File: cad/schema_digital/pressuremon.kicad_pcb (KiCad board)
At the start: 2 copper layers, 50 x 50 mm, 16 parts, among them J1 Digital Pressure 1, J2 Digital Pressure 2, Q1 BC337, U3 DS18B20

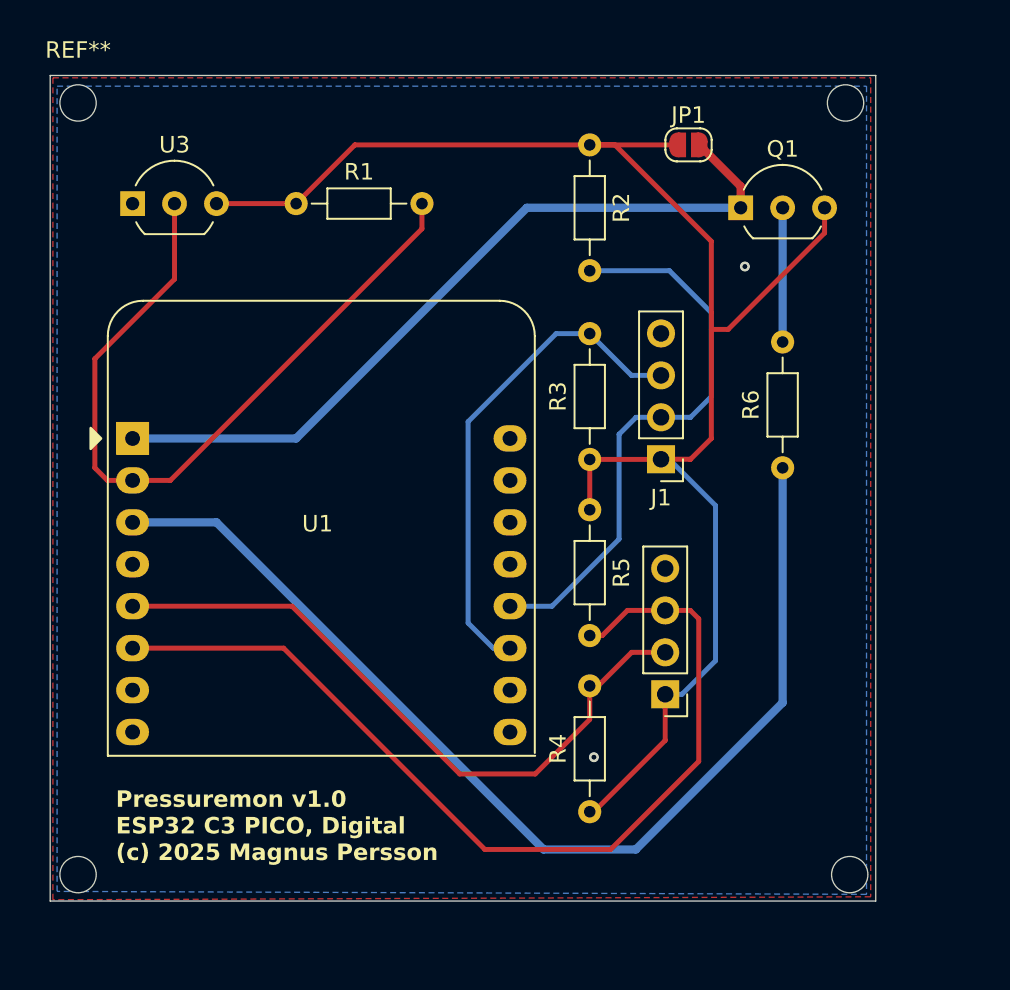
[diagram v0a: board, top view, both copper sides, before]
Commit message: Update pcb for digital sensors
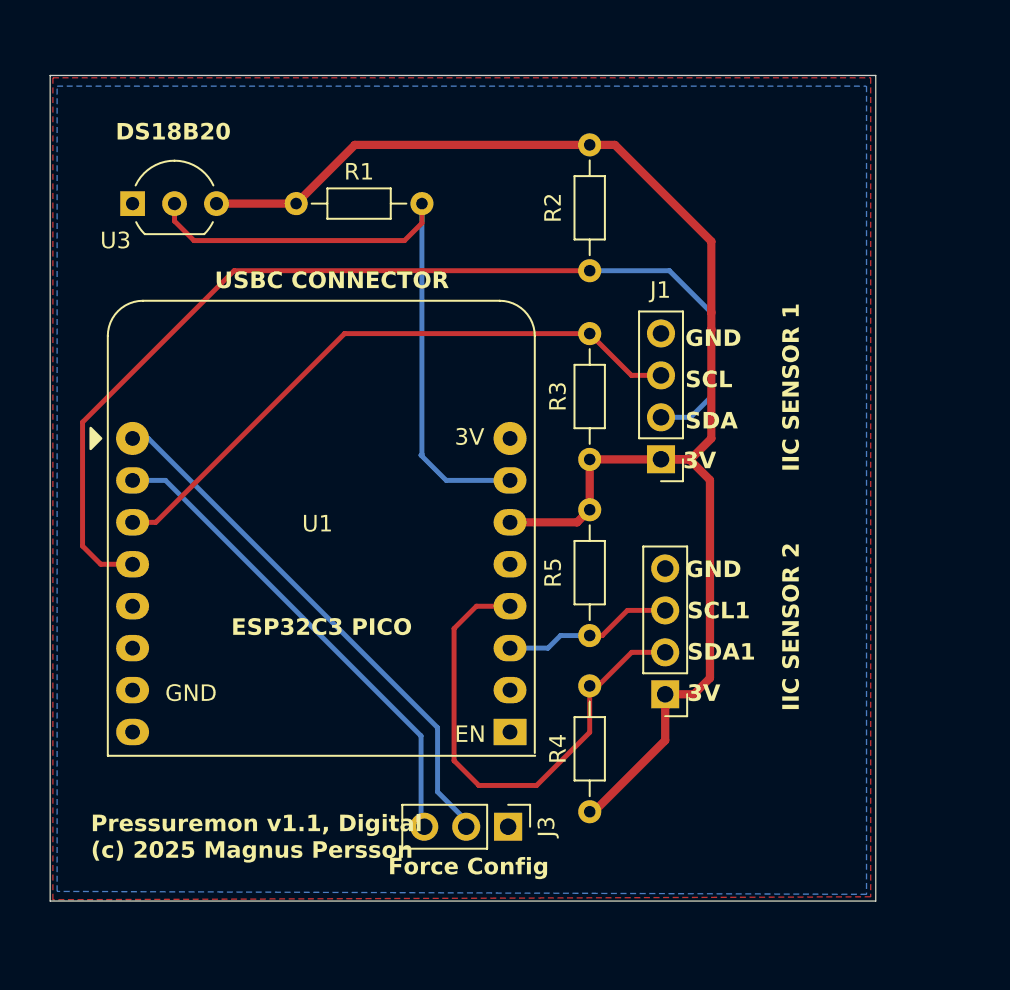
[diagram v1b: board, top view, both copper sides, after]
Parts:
- removed ? (x3): , 
- removed JP1: SolderJumper_2_Open, Jumper:SolderJumper-2_P1.3mm_Open_RoundedPad1.0x1.5mm
- removed Q1: BC337, Package_TO_SOT_THT:TO-92_Inline_Wide
- removed R6: 3.3k, Resistor_THT:R_Axial_DIN0204_L3.6mm_D1.6mm_P7.62mm_Horizontal
- removed REF**: MountingHole_2.2mm_M2, MountingHole:MountingHole_2.2mm_M2
- added J3: Force Config, Connector_PinHeader_2.54mm:PinHeader_1x03_P2.54mm_Vertical, F.Cu at (135.8, 86.0)
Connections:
- U1 pad 1: +3.3V -> unconnected-(U1-3.3V-Pad1)
- U1 pad 15: unconnected-(U1-RX-Pad15) -> Net-(J3-Pin_3)
- U1 pad 16: unconnected-(U1-TX-Pad16) -> Net-(J3-Pin_2)
- U1 pad 3: Net-(U1-4(MOSI)) -> /VCC
- U1 pad 9: +5V -> unconnected-(U1-5V-Pad9)
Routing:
- net Net-(U1-4(MOSI)): track 65.5 -> 0.00 mm
- net +3.3V: track 47.5 -> 0.00 mm
- net /SCL1: track 57.6 -> 10.3 mm
- net Net-(J3-Pin_2): track 0.00 -> 32.9 mm
- net Net-(J3-Pin_3): track 0.00 -> 30.0 mm
- net /SDA: track 34.7 -> 62.6 mm
- net /SDA1: track 40.7 -> 30.3 mm
- net /VCC: track 99.8 -> 89.7 mm
- net Net-(Q1-B): track 8.13 -> 0.00 mm
- net /SCL: track 30.3 -> 37.8 mm
- net Net-(U1-5): track 46.0 -> 39.4 mm
- net GND: vias 2 -> 0
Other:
- board text added: "3V"
- board text added: "DS18B20"
- board text added: "ESP32C3 PICO"
- board text added: "Force Config"
- board text added: "GND"
- board text added: "IIC SENSOR 1"
- board text added: "IIC SENSOR 2"
- board text added: "Pressuremon v1.1, Digital (c) 2025 Magnus Persson"
- board text added: "SCL"
- board text added: "SCL1"
- board text added: "SDA"
- board text added: "SDA1"
- board text added: "USBC CONNECTOR"
- board text removed: "Pressuremon v1.0 ESP32 C3 PICO, Digital (c) 2025 Magnus Persson"

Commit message: Update pcb
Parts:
- added ?: , , F.Cu at (156.0, 42.5)
- added ?: , , F.Cu at (110.0, 88.5)
- added ?: , , F.Cu at (156.0, 88.5)
- added REF**: MountingHole_2.2mm_M2_ISO7380, MountingHole:MountingHole_2.2mm_M2_ISO7380, F.Cu at (110.0, 42.5)
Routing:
- net /SDA1: track 30.3 -> 13.3 mm
- net Net-(U1-5): track 39.4 -> 38.5 mm
- net /SDA: track 62.6 -> 61.9 mm
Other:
- board text added: "I2C SENSOR 1"
- board text added: "I2C SENSOR 2"
- board text removed: "IIC SENSOR 1"
- board text removed: "IIC SENSOR 2"

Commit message: Update pcb to v1.2
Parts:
- removed ? (x3): , 
- removed REF**: MountingHole_2.2mm_M2_ISO7380, MountingHole:MountingHole_2.2mm_M2_ISO7380
- J1: value Digital Pressure 1 -> Conn_01x04_Pin
- J2: value Digital Pressure 2 -> Conn_01x04_Pin
- J3: value Force Config -> Conn_01x03_Pin
- R1, R2, R3, R4, R5: value 3.3k -> R
- U3: footprint Package_TO_SOT_THT:TO-92_Inline_Wide -> Package_TO_SOT_THT:TO-92_Inline
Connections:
- U1 pad 10: GND -> Net-(J3-Pin_3)
- U1 pad 11: unconnected-(U1-6-Pad11) -> /SCL
- U1 pad 12: unconnected-(U1-7(LED)-Pad12) -> /SDA
- U1 pad 13: /SDA -> unconnected-(U1-7(LED)-Pad13)
- U1 pad 14: /SCL -> unconnected-(U1-6-Pad14)
- U1 pad 15: Net-(J3-Pin_3) -> GND
- U1 pad 16: Net-(J3-Pin_2) -> unconnected-(U1-5V-Pad16)
- U1 pad 9: unconnected-(U1-5V-Pad9) -> Net-(J3-Pin_2)
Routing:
- net /SDA: track 61.9 -> 52.5 mm
- net Net-(J3-Pin_3): track 30.0 -> 21.4 mm
- net Net-(J3-Pin_2): track 32.9 -> 24.8 mm
- net /SCL: track 37.8 -> 40.9 mm
- net /VCC: track 89.7 -> 92.2 mm
- net Net-(U1-5): track 38.5 -> 40.1 mm
- net unconnected-(U1-5V-Pad16): track 0.00 -> 0.95 mm
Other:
- board text added: "Pressuremon v1.2, Digital (c) 2025 Magnus Persson"
- board text removed: "Pressuremon v1.1, Digital (c) 2025 Magnus Persson"

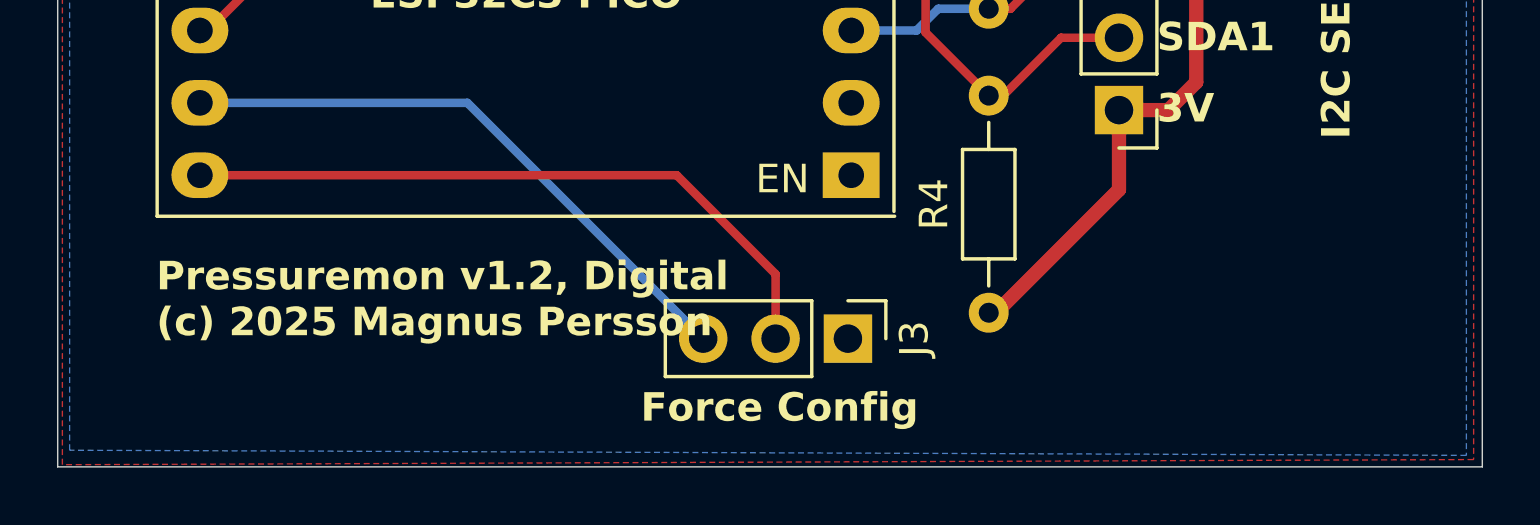
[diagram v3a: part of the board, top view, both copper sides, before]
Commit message: Updating schematic, adding off switch
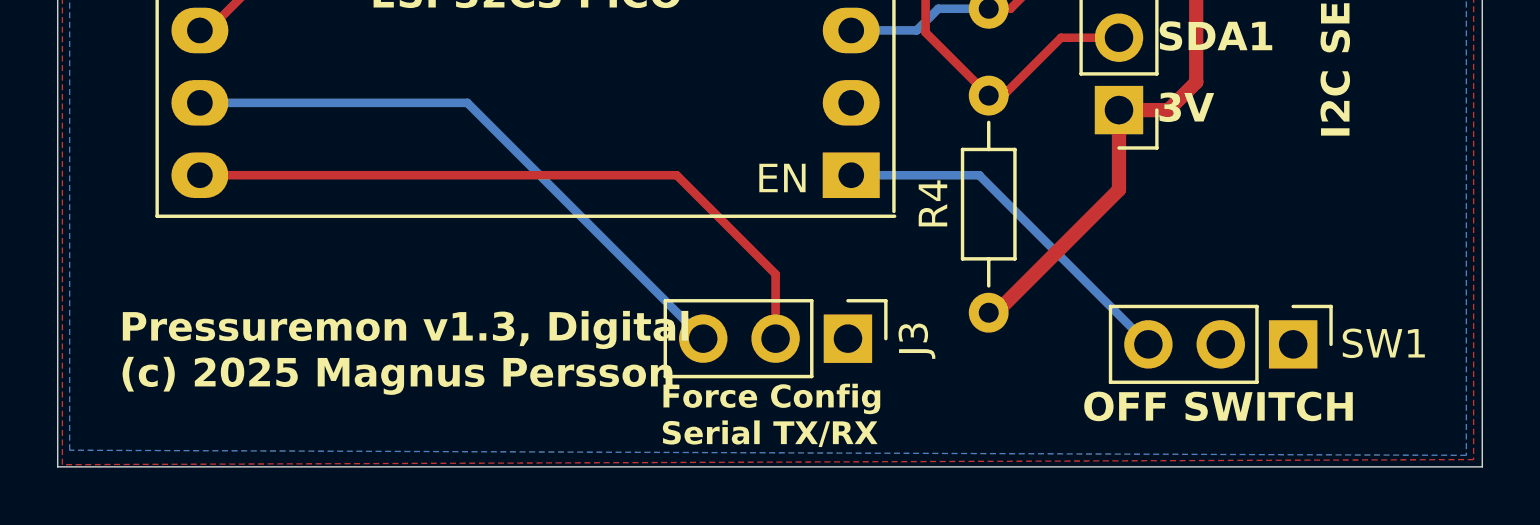
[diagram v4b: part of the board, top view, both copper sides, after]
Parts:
- added SW1: SW_SPDT, Connector_PinHeader_2.54mm:PinHeader_1x03_P2.54mm_Vertical, F.Cu at (151.4, 86.2)
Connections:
- U1 pad 8: unconnected-(U1-EN/RST-Pad8) -> Net-(SW1-C)
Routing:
- net Net-(SW1-C): track 0.00 -> 12.9 mm
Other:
- board text added: "Force Config Serial TX/RX"
- board text added: "OFF SWITCH"
- board text added: "Pressuremon v1.3, Digital (c) 2025 Magnus Persson"
- board text removed: "Force Config"
- board text removed: "Pressuremon v1.2, Digital (c) 2025 Magnus Persson"

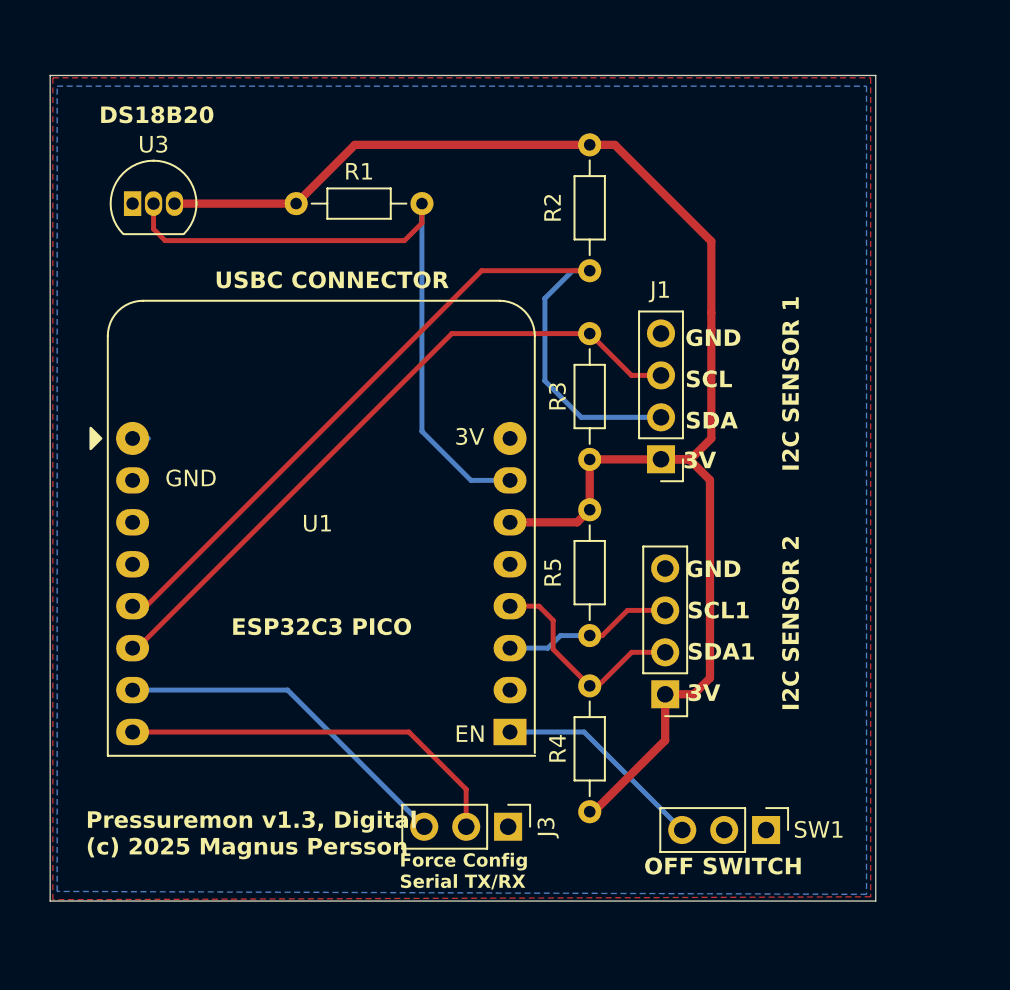
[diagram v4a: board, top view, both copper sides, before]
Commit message: Adding off switch
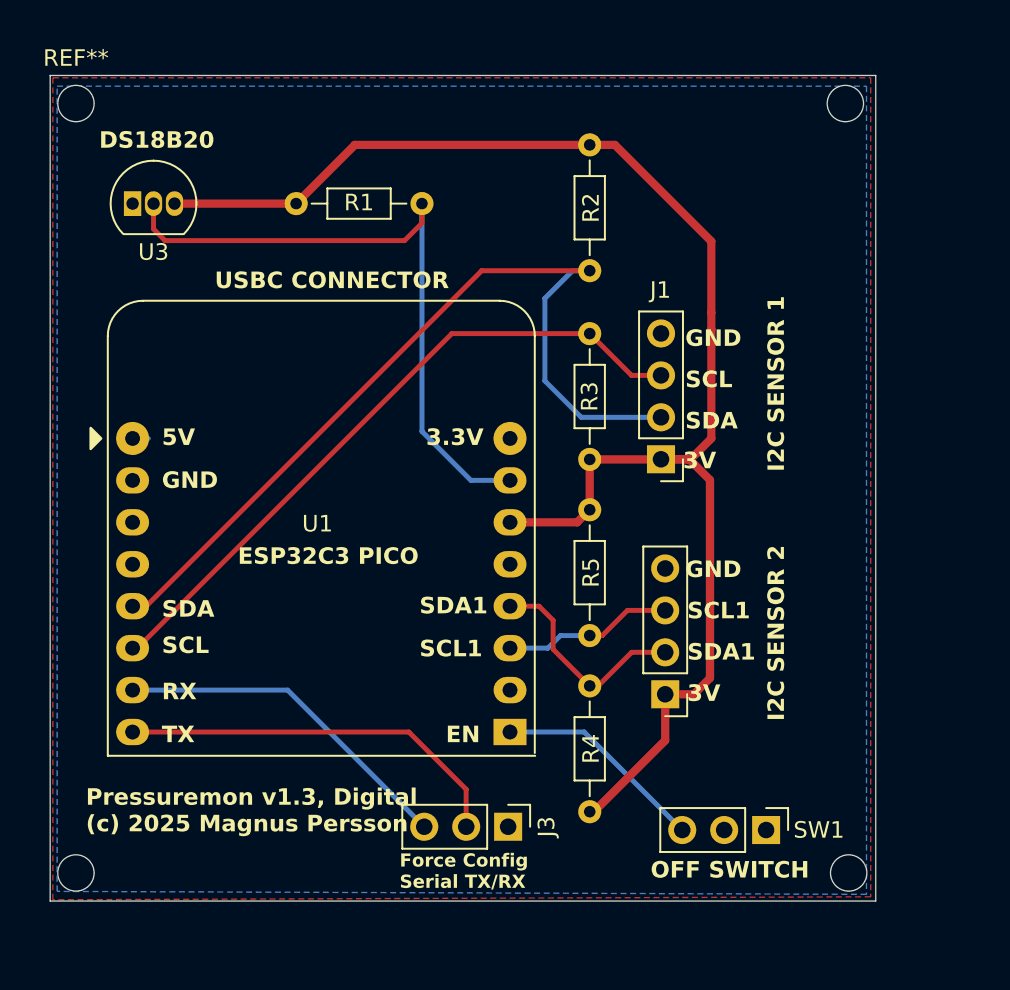
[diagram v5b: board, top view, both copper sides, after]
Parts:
- added ?: , , F.Cu at (156.4, 88.8)
- added ?: , , F.Cu at (109.6, 88.8)
- added ?: , , F.Cu at (156.2, 42.2)
- added REF**: MountingHole_2.2mm_M2_ISO7380, MountingHole:MountingHole_2.2mm_M2_ISO7380, F.Cu at (109.6, 42.2)
- R1, R2, R3, R4, R5: value R -> 3.3k
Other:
- board text added: "3.3V"
- board text added: "5V"
- board text added: "EN"
- board text added: "RX"
- board text added: "TX"

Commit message: Update pcb to v1.3
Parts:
- removed ? (x3): , 
- removed the REF** at (109.6, 42.2)
- added REF**: MountingHole_2.2mm_M2_DIN965, MountingHole:MountingHole_2.2mm_M2_DIN965, F.Cu at (109.6, 88.8)
- added REF**: MountingHole_2.2mm_M2_DIN965, MountingHole:MountingHole_2.2mm_M2_DIN965, F.Cu at (156.4, 89.0)
- added REF**: MountingHole_2.2mm_M2_DIN965, MountingHole:MountingHole_2.2mm_M2_DIN965, F.Cu at (156.4, 42.0)
- added REF**: MountingHole_2.2mm_M2_DIN965, MountingHole:MountingHole_2.2mm_M2_DIN965, F.Cu at (109.6, 42.0)
- U3: footprint Package_TO_SOT_THT:TO-92_Inline -> Package_TO_SOT_THT:TO-92L_Inline_Wide
- moved J3 43.7 mm to (153.3, 46.0)
- moved SW1 1.40 mm to (151.4, 84.8)
- moved J1 0.37 mm to (145.4, 63.7)
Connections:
- SW1 pad 1: unconnected-(SW1-A-Pad1) -> GND
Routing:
- net Net-(J3-Pin_3): track 21.4 -> 61.8 mm
- net Net-(J3-Pin_2): track 24.8 -> 64.7 mm
- net /VCC: track 92.2 -> 89.7 mm
- net Net-(U1-5): track 40.1 -> 38.3 mm
- net /SDA: track 52.5 -> 51.0 mm
- net unconnected-(U1-5V-Pad16): track 0.95 -> 0.00 mm
- net Net-(SW1-C): track 12.9 -> 12.3 mm
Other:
- board text added: "Solder the LED and BATT jumpers on the back of the esp before mounting"
- board text removed: "3.3V"
- board text removed: "EN"
- board text removed: "USBC CONNECTOR"

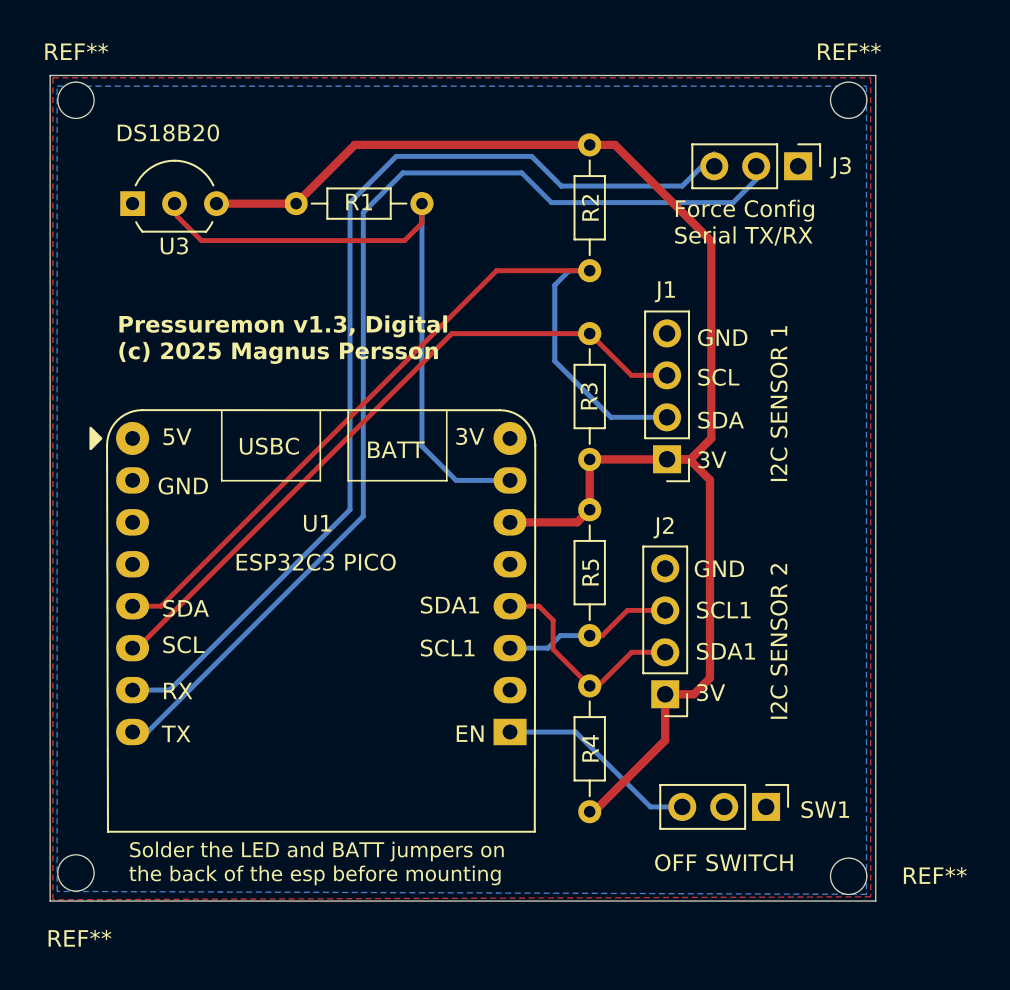
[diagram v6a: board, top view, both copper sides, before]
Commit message: Adding mounting holes to pcb
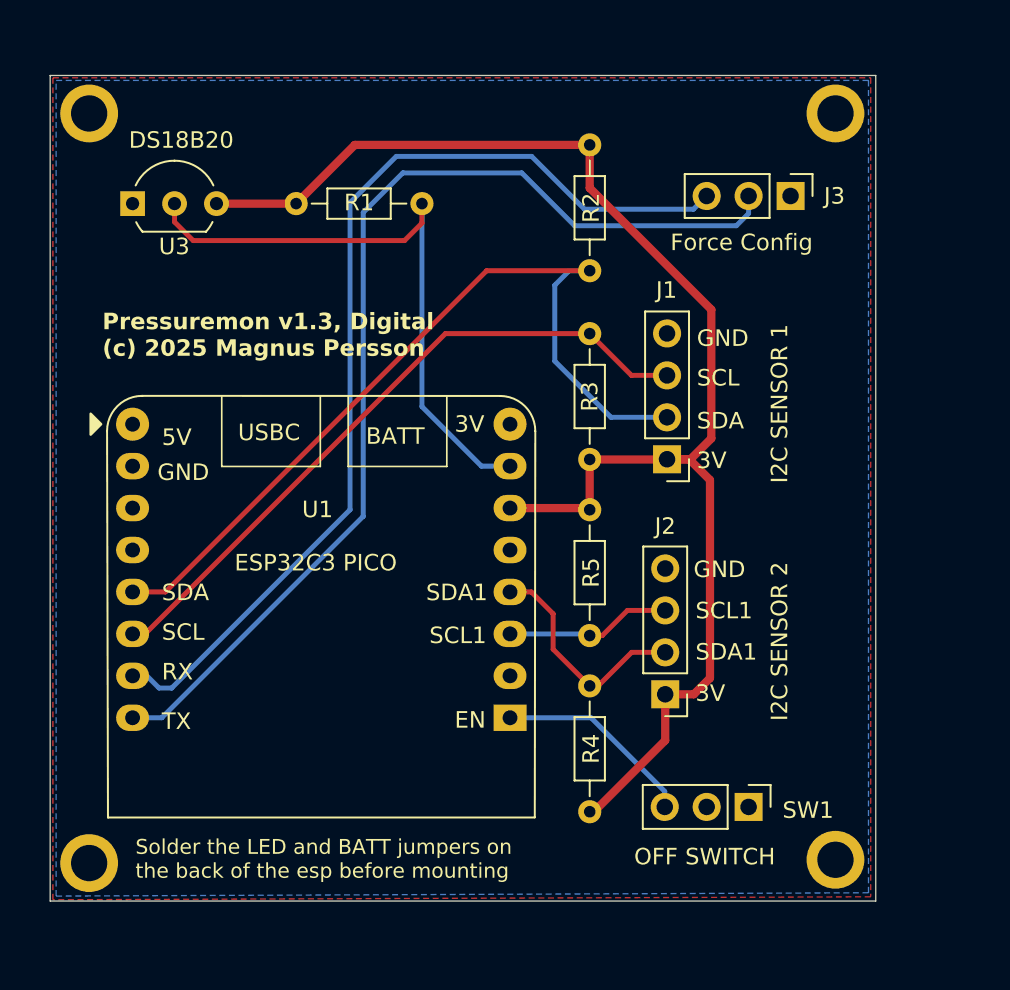
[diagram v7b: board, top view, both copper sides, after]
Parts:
- removed REF** (x4): MountingHole_2.2mm_M2_DIN965, MountingHole:MountingHole_2.2mm_M2_DIN965
- added H1: MountingHole_Pad, MountingHole:MountingHole_2.2mm_M2_ISO7380_Pad, F.Cu at (155.6, 42.8)
- added H2: MountingHole_Pad, MountingHole:MountingHole_2.2mm_M2_ISO7380_Pad, F.Cu at (110.4, 42.8)
- added H3: MountingHole_Pad, MountingHole:MountingHole_2.2mm_M2_ISO7380_Pad, F.Cu at (155.6, 88.0)
- added H4: MountingHole_Pad, MountingHole:MountingHole_2.2mm_M2_ISO7380_Pad, F.Cu at (110.4, 88.2)
- J3: value Conn_01x03_Pin -> Force Config
- moved J3 1.86 mm to (152.9, 47.8)
- moved SW1 1.06 mm to (150.3, 84.8)
- moved U1 0.86 mm to (113.0, 61.6)
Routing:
- net Net-(U1-5): track 38.3 -> 35.8 mm
- net /VCC: track 89.7 -> 87.6 mm
- net Net-(J3-Pin_3): track 61.8 -> 60.1 mm
- net /SDA: track 51.0 -> 49.8 mm
- net Net-(SW1-C): track 12.3 -> 11.6 mm
- net Net-(J3-Pin_2): track 64.7 -> 64.1 mm
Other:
- board text added: "Force Config"
- board text removed: "Force Config Serial TX/RX"
